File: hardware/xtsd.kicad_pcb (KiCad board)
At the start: 2 copper layers, 102.9 x 72.4 mm, 28 parts, among them J1 Bus_ISA_8bit_AB_Rev0, J2 SD_Card, J3 Micro_SD_Card, J4 Conn_01x02_Male, SW1 SW_DIP_x08, U1 74LS688, U2 74LS688, U3 SST39SF010, U4 74LS595, U5 74LS165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

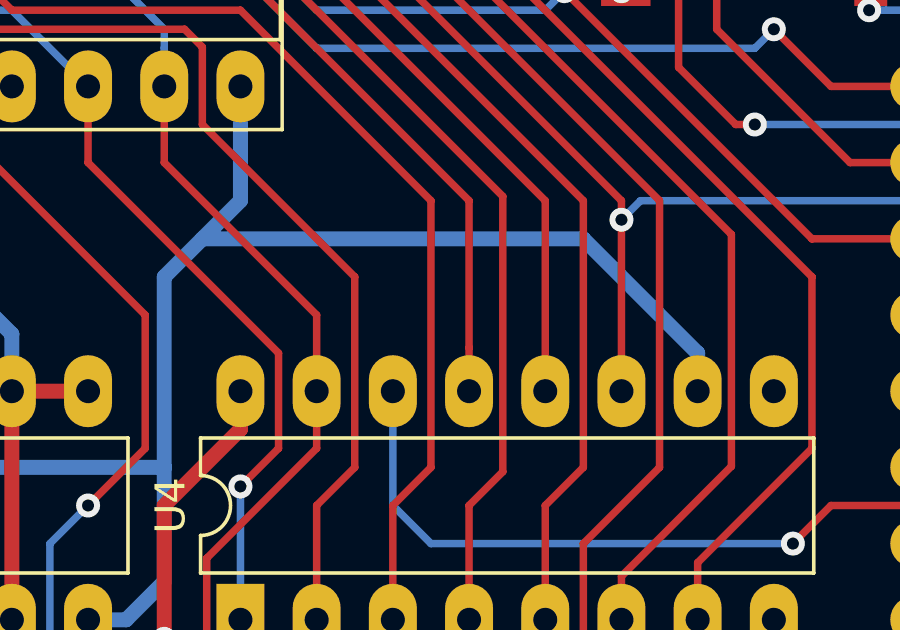
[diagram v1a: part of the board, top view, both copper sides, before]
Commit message: fix: U4 /SRCLR should be connected to VCC instead of GND
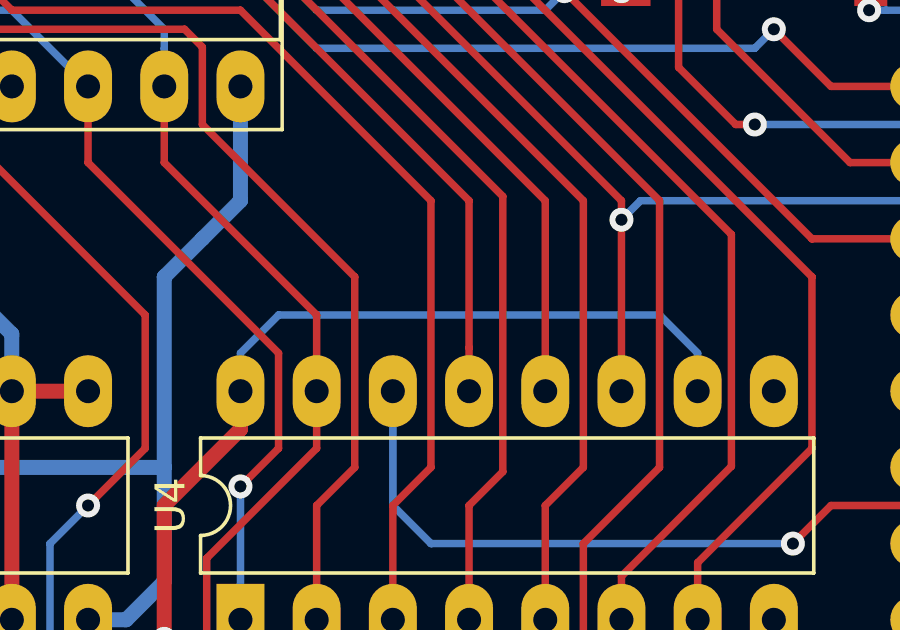
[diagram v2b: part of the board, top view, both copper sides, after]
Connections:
- U4 pad 10: GND -> VCC
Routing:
- net GND: track 282.1 -> 262.7 mm
- net VCC: track 262.0 -> 280.9 mm
